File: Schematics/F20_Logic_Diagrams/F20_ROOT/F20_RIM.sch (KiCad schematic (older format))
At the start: 2 parts, among them U24 RIM

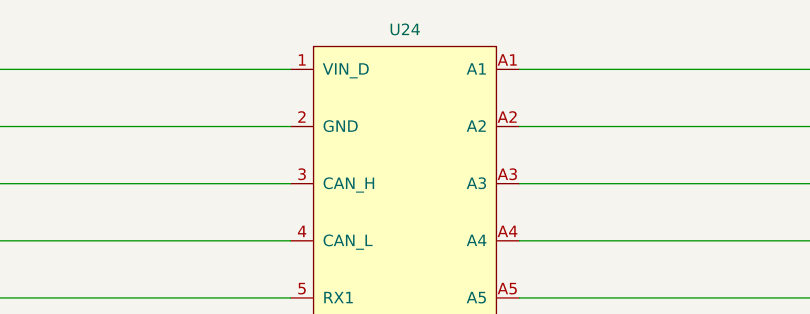
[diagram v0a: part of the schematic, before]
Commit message: Re-annotated Logic Diagrams, pulled a BOM list based on Logic Diagrams
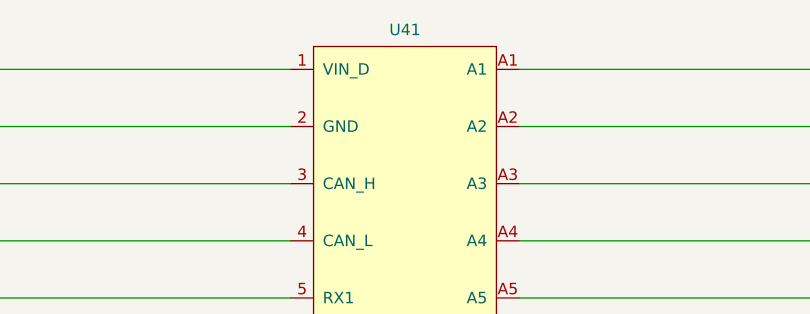
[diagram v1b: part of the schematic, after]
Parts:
- renumbered U24 to U41
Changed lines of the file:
@@
 $EndDescr
 $Comp
-L FSAE_Library:RIM U24
+L FSAE_Library:RIM U41
 U 1 1 5E4F8538
 P 5000 2000
-F 0 "U24" H 5500 2173 50  0000 C CNN
+F 0 "U41" H 5500 2173 50  0000 C CNN
 F 1 "RIM" H 5750 2150 50  0001 C CNN
 F 2 "" H 5500 3000 50  0001 C CNN
@@
 	2000 2250 2000 2500
 $Comp
-L FSAE_Library:GND_BAT #PWR017
+L FSAE_Library:GND_BAT #PWR019
 U 1 1 5E50483A
 P 2000 2500
-F 0 "#PWR017" H 2000 2250 50  0001 C CNN
+F 0 "#PWR019" H 2000 2250 50  0001 C CNN
 F 1 "GND_BAT" H 2005 2327 50  0000 C CNN
 F 2 "" H 2000 2500 50  0001 C CNN
@@
 	2000 3500 2000 4000
 $Comp
-L FSAE_Library:GND #PWR018
+L FSAE_Library:GND #PWR020
 U 1 1 5E5BE1D2
 P 2000 4000
-F 0 "#PWR018" H 2000 3800 50  0001 C CNN
+F 0 "#PWR020" H 2000 3800 50  0001 C CNN
 F 1 "GND" H 2004 3846 50  0000 C CNN
 F 2 "" H 2000 3950 50  0001 C CNN
